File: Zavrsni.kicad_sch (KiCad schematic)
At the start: 43 parts, among them K1 JST-2pin-SMD, SW1 SW_Push, SW2 SW_Push

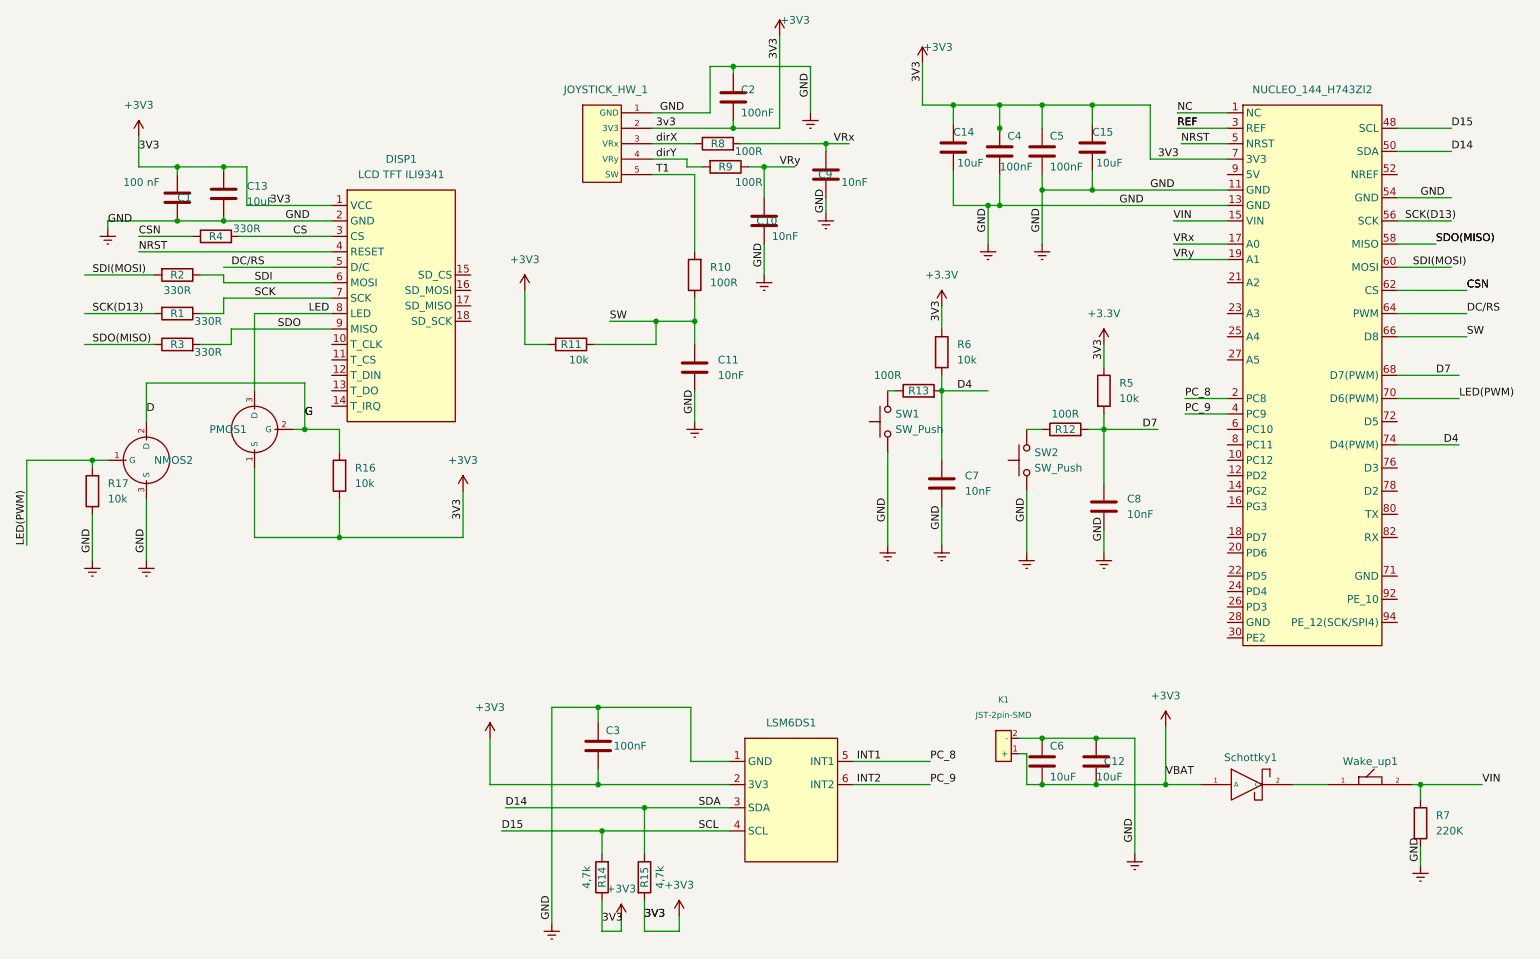
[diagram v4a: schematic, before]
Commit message: The pcb is assembled, but the pin spacing is incorrect
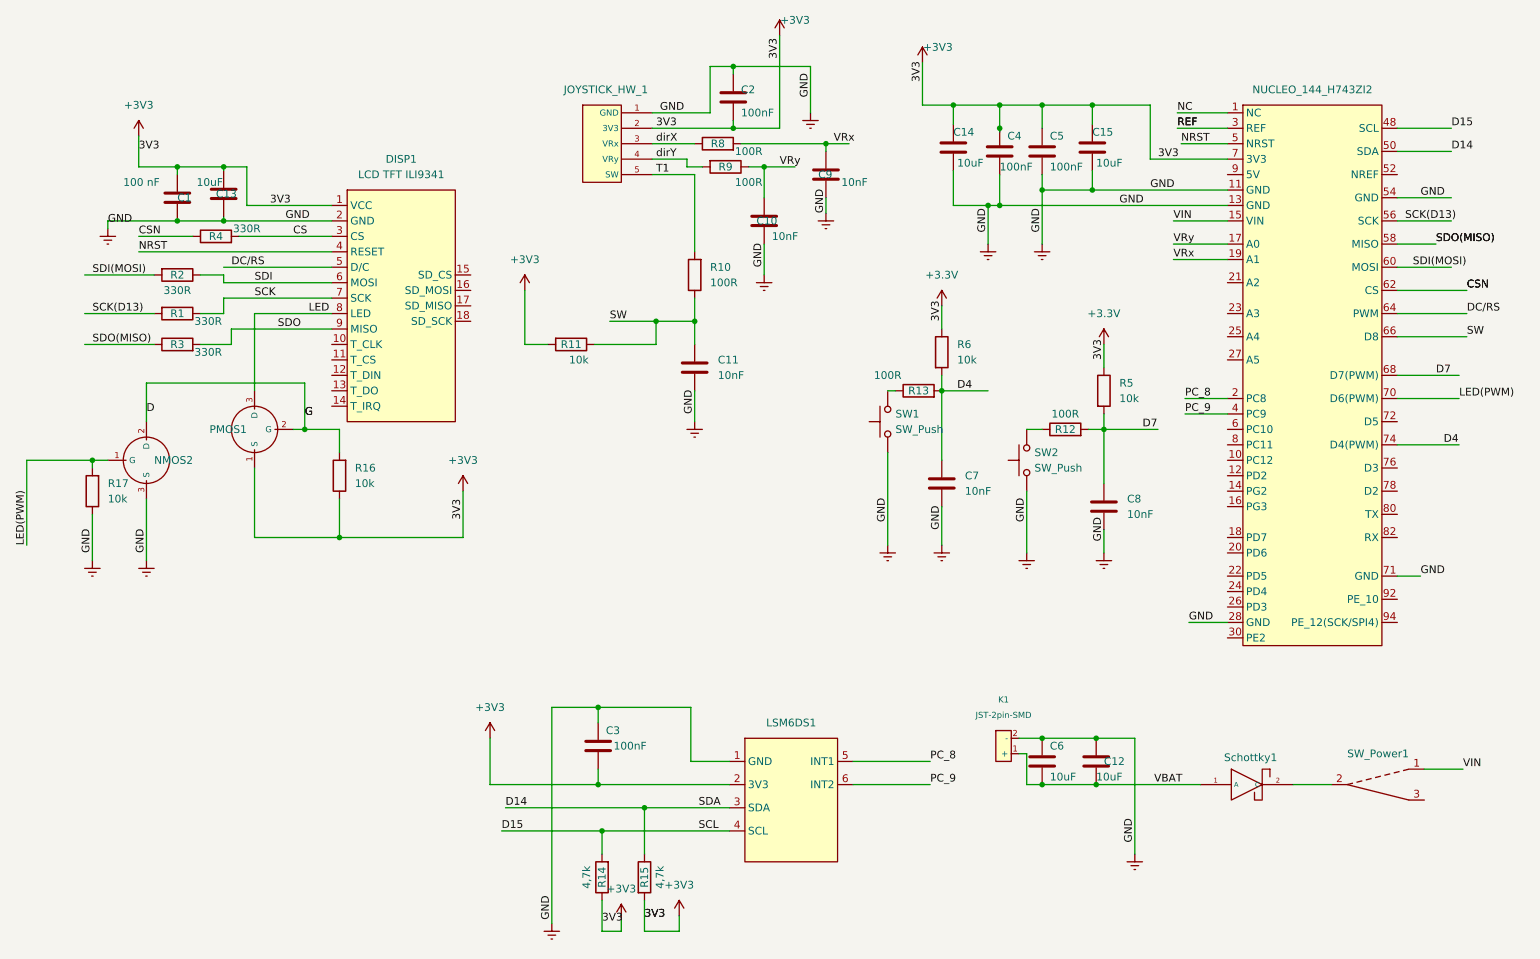
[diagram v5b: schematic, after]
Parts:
- removed R7: 220K, Resistor_SMD:R_0603_1608Metric, symbol Device:R
- renumbered Wake_up1 to SW_Power1
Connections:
- net +3.3V: no longer C12.2, C6.2, K1.1 (+), Schottky1.1 (A)
- net Earth: now also NUCLEO_144_H743ZI2.28 (GND), NUCLEO_144_H743ZI2.71 (GND)
- net VIN: now also SW_Power1.1; no longer SW_Power1.2
- net VRx: now also NUCLEO_144_H743ZI2.19 (A1); no longer NUCLEO_144_H743ZI2.17 (A0)
- net VRy: now also NUCLEO_144_H743ZI2.17 (A0); no longer NUCLEO_144_H743ZI2.19 (A1)
- net at Schottky1.2 (C): now also SW_Power1.2; no longer SW_Power1.1
- net INT1 renamed PC_8
- net INT2 renamed PC_9
- new net VBAT: C12.2, C6.2, K1.1 (+), Schottky1.1 (A)

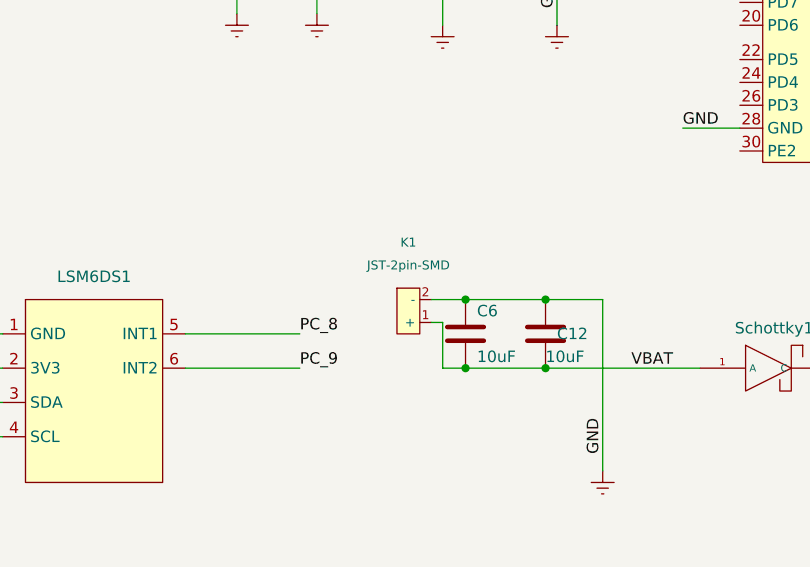
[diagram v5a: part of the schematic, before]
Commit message: The pcb is cut for the buttons on the NUCLEO board
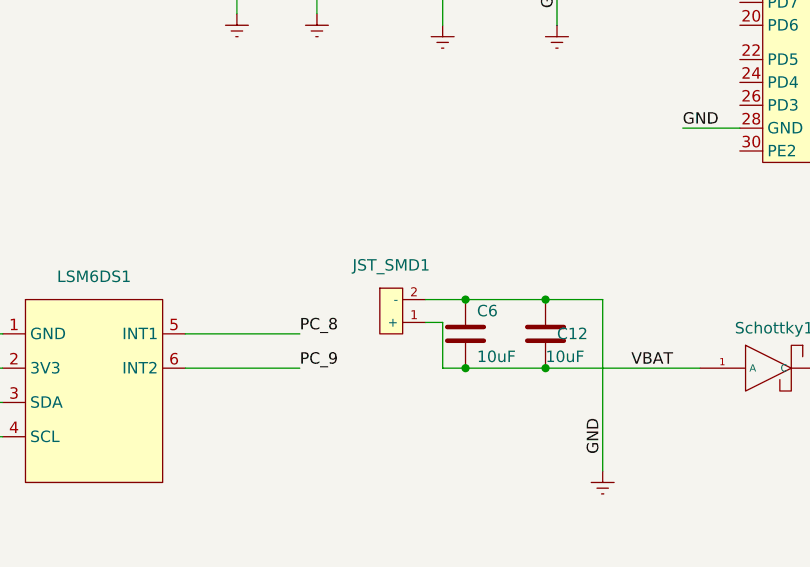
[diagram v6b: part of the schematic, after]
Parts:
- removed K1: JST-2pin-SMD, JST conector:jst connector, symbol jst-2pin-smd:JST-2pin-SMD
- added JST_SMD1: ~, JST_connector_SMD:JST_SMD, symbol JST:JST
- C12, C6: footprint Capacitor_SMD:C_0603_1608Metric -> Capacitor_SMD:C_1206_3216Metric
- SW1, SW2: footprint Button_Switch_SMD:SW_Push_1P1T_NO_6x6mm_H9.5mm -> Button_Switch_SMD:SW_SPST_SKQG_WithoutStem
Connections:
- net Earth: now also JST_SMD1.2 (-)
- net VBAT: now also JST_SMD1.1 (+)
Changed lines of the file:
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@@
     (stroke (width 0) (type default))
   )
-  (wire (pts (xy 200.66 139.7) (xy 204.47 139.7))
+  (wire (pts (xy 200.025 139.7) (xy 204.47 139.7))
     (stroke (width 0) (type default))
   )
@@
     (stroke (width 0) (type default))
   )
-  (wire (pts (xy 200.66 142.24) (xy 201.93 142.24))
+  (wire (pts (xy 200.025 142.24) (xy 201.93 142.24))
     (stroke (width 0) (type default))
   )
@@
       (effects (font (size 1.27 1.27)) (justify left))
     )
-    (property "Footprint" "Capacitor_SMD:C_0603_1608Metric" (at 214.3252 147.32 0)
+    (property "Footprint" "Capacitor_SMD:C_1206_3216Metric" (at 214.3252 147.32 0)
       (effects (font (size 1.27 1.27)) hide)
     )
@@
       (effects (font (size 1.27 1.27)) (justify left))
     )
-    (property "Footprint" "Capacitor_SMD:C_0603_1608Metric" (at 205.4352 147.32 0)
+    (property "Footprint" "Capacitor_SMD:C_1206_3216Metric" (at 205.4352 147.32 0)
       (effects (font (size 1.27 1.27)) hide)
     )
@@
       (effects (font (size 1.27 1.27)) (justify right))
     )
-    (property "Footprint" "Button_Switch_SMD:SW_Push_1P1T_NO_6x6mm_H9.5mm" (at 196.85 93.98 0)
+    (property "Footprint" "Button_Switch_SMD:SW_SPST_SKQG_WithoutStem" (at 196.85 93.98 0)
       (effects (font (size 1.27 1.27)) hide)
     )
@@
     )
   )
-  (symbol (lib_id "jst-2pin-smd:JST-2pin-SMD") (at 199.39 142.24 0) (unit 1)
-    (in_bom yes) (on_board yes) (dnp no) (fields_autoplaced)
-    (property "Reference" "K1" (at 198.12 133.35 0)
-      (effects (font (size 1 1)))
-    )
-    (property "Value" "JST-2pin-SMD" (at 198.12 135.89 0)
-      (effects (font (size 1 1)))
-    )
-    (property "Footprint" "JST conector:jst connector" (at 199.39 142.24 0)
-      (effects (font (size 1 1)) hide)
-    )
-    (property "Datasheet" "" (at 199.39 142.24 0)
-      (effects (font (size 1 1)) hide)
-    )
-    (pin "1")
-    (pin "2")
-    (instances
-      (project "Zavrsni"
-        (path "/0b0be7ad-a3a6-4dc5-99d9-af21078bf390"
-          (reference "K1") (unit 1)
-        )
-      )
-    )
-  )
   (symbol (lib_id "Device:R") (at 88.9 96.52 180) (unit 1)
     (in_bom yes) (on_board yes) (dnp no) (fields_autoplaced)
@@
         (path "/0b0be7ad-a3a6-4dc5-99d9-af21078bf390"
           (reference "C11") (unit 1)
+        )
+      )
+    )
+  )
+  (symbol (lib_id "JST:JST") (at 196.215 140.97 0) (unit 1)
+    (in_bom yes) (on_board yes) (dnp no) (fields_autoplaced)
+    (property "Reference" "JST_SMD1" (at 196.215 135.89 0)
+      (effects (font (size 1.27 1.27)))
+    )
+    (property "Value" "~" (at 196.215 140.97 0)
+      (effects (font (size 1.27 1.27)))
+    )
+    (property "Footprint" "JST_connector_SMD:JST_SMD" (at 196.215 140.97 0)
+      (effects (font (size 1.27 1.27)) hide)
+    )
+    (property "Datasheet" "" (at 196.215 140.97 0)
+      (effects (font (size 1.27 1.27)) hide)
+    )
+    (pin "1")
+    (pin "2")
+    (instances
+      (project "Zavrsni"
+        (path "/0b0be7ad-a3a6-4dc5-99d9-af21078bf390"
+          (reference "JST_SMD1") (unit 1)
         )
       )
@@
       (effects (font (size 1.27 1.27)) (justify right))
     )
-    (property "Footprint" "Button_Switch_SMD:SW_Push_1P1T_NO_6x6mm_H9.5mm" (at 173.99 87.63 0)
-      (effects (font (size 1.27 1.27)) hide)
-    )
+    (property "Footprint" "Button_Switch_SMD:SW_SPST_SKQG_WithoutStem" (at 173.99 87.63 0)
+      (effects (font (size 1.27 1.27)) hide)
+    )
